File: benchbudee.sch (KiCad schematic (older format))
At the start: 0 parts

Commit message: Module 2 Unit 14
Defining Your Inputs and Outputs
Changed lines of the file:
@@
 LIBS:contrib
 LIBS:valves
-LIBS:benchbudee-block-cache
+LIBS:benchbudee-cache
 EELAYER 27 0
 EELAYER END
@@
 Sheet 1 8
 Title ""
-Date "1 feb 2014"
+Date "2 feb 2014"
 Rev ""
 Comp ""
@@
 $EndDescr
 $Sheet
-S 700  5100 3300 2250
+S 750  3950 3300 3000
 U 52ED26CD
 F0 "arduino" 50
 F1 "arduino.sch" 50
+F2 "Relay+" O R 4050 6700 60
+F3 "Relay-" I R 4050 6500 60
+F4 "MOSI" O R 4050 5500 60
+F5 "MISO" I R 4050 5700 60
+F6 "SCLK" O R 4050 5900 60
+F7 "CS_N" O R 4050 6100 60
+F8 "LED_EN" O R 4050 4900 60
+F9 "LED_FREQ" O R 4050 5100 60
+F10 "FAN_EN" O R 4050 4300 60
+F11 "TACH_MEAS" I R 4050 4500 60
 $EndSheet
 $Sheet
@@
 F2 "tc in +" I R 8250 4200 60
 F3 "tc in -" I R 8250 4400 60
+F4 "MOSI" I L 5550 4200 60
+F5 "MISO" O L 5550 4400 60
+F6 "SCLK" I L 5550 4600 60
+F7 "CS_N" I L 5550 4800 60
 $EndSheet
 $Sheet
@@
 F0 "relay" 50
 F1 "relay.sch" 50
+F2 "DIN+" I L 5550 5900 60
+F3 "DIN-" O L 5550 6100 60
+F4 "Relay+" I R 8250 5900 60
+F5 "Relay-" O R 8250 6100 60
 $EndSheet
 $Sheet
@@
 F0 "led driver" 50
 F1 "led driver.sch" 50
+F2 "EN" I L 5550 2600 60
+F3 "FREQ" I L 5550 2800 60
+F4 "String+" O R 8250 2600 60
+F5 "String-" I R 8250 2800 60
 $EndSheet
 $Sheet
@@
 F0 "fan controller" 50
 F1 "fan controller.sch" 50
+F2 "Power+" O R 8250 900 60
+F3 "Power-" I R 8250 1100 60
+F4 "Tach_out" O L 5550 1100 60
+F5 "Tach" I R 8250 1300 60
+F6 "Fan_in" I L 5550 900 60
 $EndSheet
 $Sheet

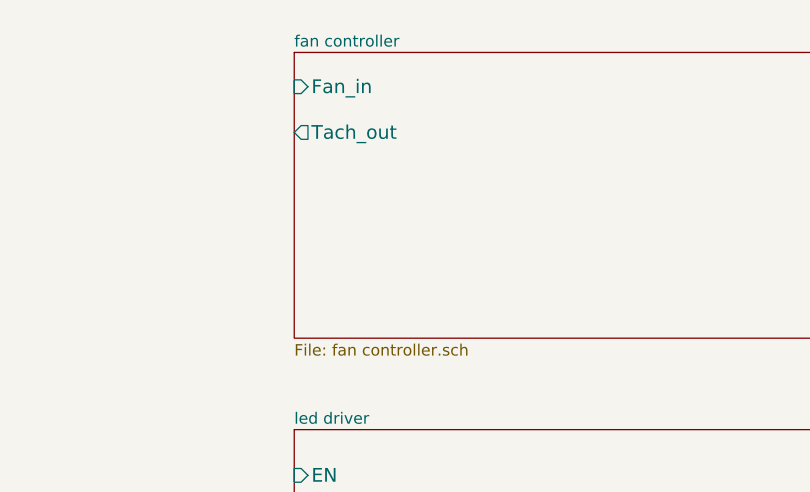
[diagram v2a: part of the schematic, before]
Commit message: Module 3 unit 4
Understanding The Current/Fan Driver Module
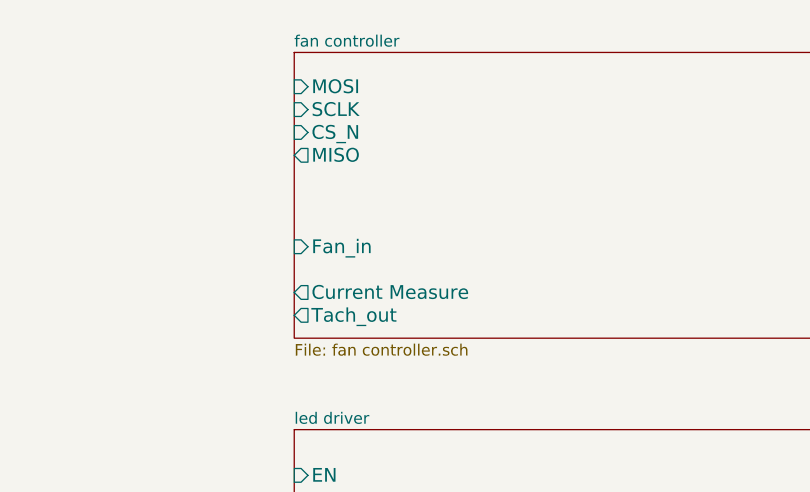
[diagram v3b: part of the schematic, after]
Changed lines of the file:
@@
 Sheet 1 8
 Title ""
-Date "8 feb 2014"
+Date "10 feb 2014"
 Rev ""
 Comp ""
@@
 F2 "Power+" O R 8250 900 60
 F3 "Power-" I R 8250 1100 60
-F4 "Tach_out" O L 5550 1100 60
+F4 "Tach_out" O L 5550 1900 60
 F5 "Tach" I R 8250 1300 60
-F6 "Fan_in" I L 5550 900 60
+F6 "Fan_in" I L 5550 1600 60
+F7 "Current Measure" O L 5550 1800 60
+F8 "MOSI" I L 5550 900 60
+F9 "MISO" O L 5550 1200 60
+F10 "CS_N" I L 5550 1100 60
+F11 "SCLK" I L 5550 1000 60
 $EndSheet
 $Sheet

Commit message: Module 3 Unit 5
Understanding The Relay Module
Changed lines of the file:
@@
 LIBS:contrib
 LIBS:valves
+LIBS:benchbudee
 LIBS:benchbudee-cache
 EELAYER 27 0
@@
 F2 "DIN+" I L 5550 5900 60
 F3 "DIN-" O L 5550 6100 60
-F4 "Relay+" I R 8250 5900 60
-F5 "Relay-" O R 8250 6100 60
+F4 "NC" B R 8250 6300 60
+F5 "NO" B R 8250 6500 60
+F6 "COM" B R 8250 6700 60
 $EndSheet
 $Sheet

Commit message: Module 3 Unit 6
Understanding The Power Protection And Filtering Module
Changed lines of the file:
@@
 $Descr A4 11693 8268
 encoding utf-8
-Sheet 1 8
+Sheet 1 9
 Title ""
 Date "10 feb 2014"
@@
 $EndSheet
 $Sheet
-S 5550 4050 2700 1250
+S 6600 4100 2700 1250
 U 52ED2725
 F0 "thermocouple" 50
 F1 "thermocouple.sch" 50
-F2 "tc in +" I R 8250 4200 60
-F3 "tc in -" I R 8250 4400 60
-F4 "MOSI" I L 5550 4200 60
-F5 "MISO" O L 5550 4400 60
-F6 "SCLK" I L 5550 4600 60
-F7 "CS_N" I L 5550 4800 60
+F2 "tc in +" I R 9300 4250 60
+F3 "tc in -" I R 9300 4450 60
+F4 "MOSI" I L 6600 4250 60
+F5 "MISO" O L 6600 4450 60
+F6 "SCLK" I L 6600 4650 60
+F7 "CS_N" I L 6600 4850 60
 $EndSheet
 $Sheet
-S 5550 5700 2700 1250
+S 6600 5750 2700 1250
 U 52ED273F
 F0 "relay" 50
 F1 "relay.sch" 50
-F2 "DIN+" I L 5550 5900 60
-F3 "DIN-" O L 5550 6100 60
-F4 "NC" B R 8250 6300 60
-F5 "NO" B R 8250 6500 60
-F6 "COM" B R 8250 6700 60
+F2 "DIN+" I L 6600 5950 60
+F3 "DIN-" O L 6600 6150 60
+F4 "NC" B R 9300 6350 60
+F5 "NO" B R 9300 6550 60
+F6 "COM" B R 9300 6750 60
 $EndSheet
 $Sheet
-S 700  700  3400 1900
+S 700  700  3350 1900
 U 52ED276F
 F0 "power" 50
@@
 $EndSheet
 $Sheet
-S 5550 2400 2700 1250
+S 6600 2450 2700 1250
 U 52ED27AA
 F0 "led driver" 50
 F1 "led driver.sch" 50
-F2 "EN" I L 5550 2600 60
-F3 "FREQ" I L 5550 2800 60
-F4 "String+" O R 8250 2600 60
-F5 "String-" I R 8250 2800 60
+F2 "EN" I L 6600 2650 60
+F3 "FREQ" I L 6600 2850 60
+F4 "String+" O R 9300 2650 60
+F5 "String-" I R 9300 2850 60
 $EndSheet
 $Sheet
-S 5550 750  2700 1250
+S 6600 800  2700 1250
 U 52ED27C5
 F0 "fan controller" 50
 F1 "fan controller.sch" 50
-F2 "Power+" O R 8250 900 60
-F3 "Power-" I R 8250 1100 60
-F4 "Tach_out" O L 5550 1900 60
-F5 "Tach" I R 8250 1300 60
-F6 "Fan_in" I L 5550 1600 60
-F7 "Current Measure" O L 5550 1800 60
-F8 "MOSI" I L 5550 900 60
-F9 "MISO" O L 5550 1200 60
-F10 "CS_N" I L 5550 1100 60
-F11 "SCLK" I L 5550 1000 60
+F2 "Power+" O R 9300 950 60
+F3 "Power-" I R 9300 1150 60
+F4 "Tach_out" O L 6600 1950 60
+F5 "Tach" I R 9300 1350 60
+F6 "Fan_in" I L 6600 1650 60
+F7 "Current Measure" O L 6600 1850 60
+F8 "MOSI" I L 6600 950 60
+F9 "MISO" O L 6600 1250 60
+F10 "CS_N" I L 6600 1150 60
+F11 "SCLK" I L 6600 1050 60
 $EndSheet
 $Sheet
-S 9500 750  1000 6200
+S 9900 800  1000 6200
 U 52ED27F4
 F0 "terminal block" 50
 F1 "terminal block.sch" 50
 $EndSheet
+$Sheet
+S 4300 700  2100 1900
+U 52F95312
+F0 "power adjustment monitor" 50
+F1 "power adjustment monitor.sch" 50
+$EndSheet
 $EndSCHEMATC

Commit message: Module 3 Unit 7
Understanding The Power Control, Conditioning And Monitoring Module
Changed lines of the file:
@@
 Sheet 1 9
 Title ""
-Date "10 feb 2014"
+Date "15 feb 2014"
 Rev ""
 Comp ""
@@
 $EndSheet
 $Sheet
-S 6600 4100 2700 1250
+S 6600 4450 2650 900
 U 52ED2725
 F0 "thermocouple" 50
 F1 "thermocouple.sch" 50
-F2 "tc in +" I R 9300 4250 60
-F3 "tc in -" I R 9300 4450 60
-F4 "MOSI" I L 6600 4250 60
-F5 "MISO" O L 6600 4450 60
-F6 "SCLK" I L 6600 4650 60
-F7 "CS_N" I L 6600 4850 60
+F2 "tc in +" I R 9250 4600 60
+F3 "tc in -" I R 9250 4800 60
+F4 "MOSI" I L 6600 4600 60
+F5 "MISO" O L 6600 4800 60
+F6 "SCLK" I L 6600 5000 60
+F7 "CS_N" I L 6600 5200 60
 $EndSheet
 $Sheet
-S 6600 5750 2700 1250
+S 6600 6050 2700 750
 U 52ED273F
 F0 "relay" 50
 F1 "relay.sch" 50
-F2 "DIN+" I L 6600 5950 60
-F3 "DIN-" O L 6600 6150 60
-F4 "NC" B R 9300 6350 60
-F5 "NO" B R 9300 6550 60
-F6 "COM" B R 9300 6750 60
+F2 "DIN+" I L 6600 6250 60
+F3 "DIN-" O L 6600 6450 60
+F4 "NC" B R 9300 6200 60
+F5 "NO" B R 9300 6400 60
+F6 "COM" B R 9300 6600 60
 $EndSheet
 $Sheet
@@
 $EndSheet
 $Sheet
-S 6600 2450 2700 1250
+S 6600 3050 2700 650
 U 52ED27AA
 F0 "led driver" 50
 F1 "led driver.sch" 50
-F2 "EN" I L 6600 2650 60
-F3 "FREQ" I L 6600 2850 60
-F4 "String+" O R 9300 2650 60
-F5 "String-" I R 9300 2850 60
+F2 "EN" I L 6600 3250 60
+F3 "FREQ" I L 6600 3450 60
+F4 "String+" O R 9300 3250 60
+F5 "String-" I R 9300 3450 60
 $EndSheet
 $Sheet
@@
 $EndSheet
 $Sheet
-S 4300 700  2100 1900
+S 4300 700  1800 1300
 U 52F95312
 F0 "power adjustment monitor" 50
 F1 "power adjustment monitor.sch" 50
+F2 "3V3_MON" O L 4300 1300 60
+F3 "5V_MON" O L 4300 1400 60
+F4 "V+ADJ_MON" O L 4300 1600 60
+F5 "V-ADJ_MON" O L 4300 1700 60
+F6 "V+CURRENT_MON" O L 4300 1800 60
+F7 "V-CURRENT_MON" O L 4300 1900 60
+F8 "V+ADJ" O R 6100 1300 60
+F9 "V-ADJ" O R 6100 1500 60
 $EndSheet
 $EndSCHEMATC

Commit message: Module 3 Unit 8
Understanding The LED Driver Module
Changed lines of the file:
@@
 F0 "led driver" 50
 F1 "led driver.sch" 50
-F2 "EN" I L 6600 3250 60
-F3 "FREQ" I L 6600 3450 60
-F4 "String+" O R 9300 3250 60
-F5 "String-" I R 9300 3450 60
+F2 "String+" O R 9300 3250 60
+F3 "String-" I R 9300 3450 60
+F4 "LED_EN_PWM" I L 6600 3250 60
 $EndSheet
 $Sheet

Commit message: Module 3 Unit 9
Understanding The Arduino Module
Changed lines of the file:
@@
 Sheet 1 9
 Title ""
-Date "15 feb 2014"
+Date "16 feb 2014"
 Rev ""
 Comp ""
@@
 $EndDescr
 $Sheet
-S 750  3950 3300 3000
+S 700  3050 3300 3750
 U 52ED26CD
 F0 "arduino" 50
 F1 "arduino.sch" 50
-F2 "Relay+" O R 4050 6700 60
-F3 "Relay-" I R 4050 6500 60
-F4 "MOSI" O R 4050 5500 60
-F5 "MISO" I R 4050 5700 60
-F6 "SCLK" O R 4050 5900 60
-F7 "CS_N" O R 4050 6100 60
-F8 "LED_EN" O R 4050 4900 60
-F9 "LED_FREQ" O R 4050 5100 60
-F10 "FAN_EN" O R 4050 4300 60
-F11 "TACH_MEAS" I R 4050 4500 60
-$EndSheet
-$Sheet
-S 6600 4450 2650 900
-U 52ED2725
-F0 "thermocouple" 50
-F1 "thermocouple.sch" 50
-F2 "tc in +" I R 9250 4600 60
-F3 "tc in -" I R 9250 4800 60
-F4 "MOSI" I L 6600 4600 60
-F5 "MISO" O L 6600 4800 60
-F6 "SCLK" I L 6600 5000 60
-F7 "CS_N" I L 6600 5200 60
+F2 "MOSI" O R 4000 3700 60
+F3 "MISO" I R 4000 3800 60
+F4 "SCLK" O R 4000 3900 60
+F5 "TACH_MEAS" I R 4000 4300 60
+F6 "Relay+" O R 4000 6500 60
+F7 "Relay-" O R 4000 6700 60
+F8 "Fan_En_N" O R 4000 4200 60
+F9 "Current_Measure" I R 4000 4400 60
+F10 "V+ADJ_MON" I R 4000 3200 60
+F11 "V-ADJ_MON" I R 4000 3300 60
+F12 "LED_EN_PWM" O R 4000 5300 60
+F13 "DAC_CS_N" O R 4000 4100 60
+F14 "ADC_CS_N" O R 4000 4000 60
 $EndSheet
 $Sheet
@@
 F0 "relay" 50
 F1 "relay.sch" 50
-F2 "DIN+" I L 6600 6250 60
-F3 "DIN-" O L 6600 6450 60
-F4 "NC" B R 9300 6200 60
-F5 "NO" B R 9300 6400 60
-F6 "COM" B R 9300 6600 60
+F2 "RELAY_NC" B R 9300 6400 60
+F3 "RELAY_NO" B R 9300 6600 60
+F4 "RELAY_COM" B R 9300 6200 60
+F5 "Relay+" I L 6600 6500 60
+F6 "Relay-" O L 6600 6700 60
 $EndSheet
 $Sheet
@@
 $EndSheet
 $Sheet
-S 6600 3050 2700 650
+S 6600 5050 2700 650
 U 52ED27AA
 F0 "led driver" 50
 F1 "led driver.sch" 50
-F2 "String+" O R 9300 3250 60
-F3 "String-" I R 9300 3450 60
-F4 "LED_EN_PWM" I L 6600 3250 60
-$EndSheet
-$Sheet
-S 6600 800  2700 1250
+F2 "LED_EN_PWM" I L 6600 5300 60
+F3 "LED_String+" O R 9300 5300 60
+F4 "LED_String-" O R 9300 5500 60
+$EndSheet
+$Sheet
+S 6600 3050 2700 1550
 U 52ED27C5
 F0 "fan controller" 50
 F1 "fan controller.sch" 50
-F2 "Power+" O R 9300 950 60
-F3 "Power-" I R 9300 1150 60
-F4 "Tach_out" O L 6600 1950 60
-F5 "Tach" I R 9300 1350 60
-F6 "Fan_in" I L 6600 1650 60
-F7 "Current Measure" O L 6600 1850 60
-F8 "MOSI" I L 6600 950 60
-F9 "MISO" O L 6600 1250 60
-F10 "CS_N" I L 6600 1150 60
-F11 "SCLK" I L 6600 1050 60
-$EndSheet
-$Sheet
-S 9900 800  1000 6200
+F2 "MOSI" I L 6600 3200 60
+F3 "MISO" O L 6600 3300 60
+F4 "CS_N" I L 6600 3500 60
+F5 "SCLK" I L 6600 3400 60
+F6 "Fan_Out+" O R 9300 3200 60
+F7 "Tach_In" I R 9300 3600 60
+F8 "Tach_Meas" O L 6600 4300 60
+F9 "Fan_En_N" I L 6600 4200 60
+F10 "Current_Measure" O L 6600 4400 60
+F11 "Fan_Out-" O R 9300 3400 60
+$EndSheet
+$Sheet
+S 9900 800  1000 6000
 U 52ED27F4
 F0 "terminal block" 50
 F1 "terminal block.sch" 50
-$EndSheet
-$Sheet
-S 4300 700  1800 1300
+F2 "Tach_In" O L 9900 3600 60
+F3 "LED_String+" O L 9900 5300 60
+F4 "LED_String-" O L 9900 5500 60
+F5 "Fan_Out+" O L 9900 3200 60
+F6 "Fan_Out-" O L 9900 3400 60
+F7 "V+ADJ" I L 9900 1150 60
+F8 "V-ADJ" I L 9900 1350 60
+F9 "TC_IN+" I L 9900 2100 60
+F10 "TC_IN-" I L 9900 2300 60
+F11 "RELAY_COM" B L 9900 6200 60
+F12 "RELAY_NC" B L 9900 6400 60
+F13 "RELAY_NO" B L 9900 6600 60
+$EndSheet
+$Sheet
+S 6600 800  2700 900
 U 52F95312
 F0 "power adjustment monitor" 50
 F1 "power adjustment monitor.sch" 50
-F2 "3V3_MON" O L 4300 1300 60
-F3 "5V_MON" O L 4300 1400 60
-F4 "V+ADJ_MON" O L 4300 1600 60
-F5 "V-ADJ_MON" O L 4300 1700 60
-F6 "V+CURRENT_MON" O L 4300 1800 60
-F7 "V-CURRENT_MON" O L 4300 1900 60
-F8 "V+ADJ" O R 6100 1300 60
-F9 "V-ADJ" O R 6100 1500 60
-$EndSheet
+F2 "3V3_MON" O L 6600 900 60
+F3 "5V_MON" O L 6600 1000 60
+F4 "V+ADJ_MON" O L 6600 1200 60
+F5 "V-ADJ_MON" O L 6600 1300 60
+F6 "V+CURRENT_MON" O L 6600 1400 60
+F7 "V-CURRENT_MON" O L 6600 1500 60
+F8 "V+ADJ" O R 9300 1150 60
+F9 "V-ADJ" O R 9300 1350 60
+$EndSheet
+$Sheet
+S 6600 1950 2700 900
+U 52ED2725
+F0 "thermocouple" 50
+F1 "thermocouple.sch" 50
+F2 "MOSI" I L 6600 2100 60
+F3 "MISO" O L 6600 2200 60
+F4 "SCLK" I L 6600 2300 60
+F5 "CS_N" I L 6600 2400 60
+F6 "TC_IN+" I R 9300 2100 60
+F7 "TC_IN-" I R 9300 2300 60
+$EndSheet
+Wire Wire Line
+	9300 6200 9900 6200
+Wire Wire Line
+	9900 6400 9300 6400
+Wire Wire Line
+	9300 6600 9900 6600
+Wire Wire Line
+	9300 1150 9900 1150
+Wire Wire Line
+	9900 1350 9300 1350
+Wire Wire Line
+	9300 5300 9900 5300
+Wire Wire Line
+	9300 5500 9900 5500
+Wire Wire Line
+	4000 3200 4500 3200
+Wire Wire Line
+	4500 3200 4500 1200
+Wire Wire Line
+	4500 1200 6600 1200
+Wire Wire Line
+	6600 1300 4600 1300
+Wire Wire Line
+	4600 1300 4600 3300
+Wire Wire Line
+	4600 3300 4000 3300
+Wire Wire Line
+	9900 2100 9300 2100
+Wire Wire Line
+	9300 2300 9900 2300
+Wire Wire Line
+	9900 3200 9300 3200
+Wire Wire Line
+	9300 3400 9900 3400
+Wire Wire Line
+	9900 3600 9300 3600
+Wire Wire Line
+	4000 3700 4700 3700
+Wire Wire Line
+	4700 3700 4700 2100
+Wire Wire Line
+	4700 2100 6600 2100
+Wire Wire Line
+	6600 2200 4800 2200
+Wire Wire Line
+	4800 2200 4800 3800
+Wire Wire Line
+	4800 3800 4000 3800
+Wire Wire Line
+	4000 3900 4900 3900
+Wire Wire Line
+	4900 3900 4900 2300
+Wire Wire Line
+	4900 2300 6600 2300
+Wire Wire Line
+	4000 4200 6600 4200
+Wire Wire Line
+	4000 4300 6600 4300
+Wire Wire Line
+	4000 4400 6600 4400
+Wire Wire Line
+	6600 3200 4700 3200
+Connection ~ 4700 3200
+Wire Wire Line
+	6600 3300 4800 3300
+Connection ~ 4800 3300
+Wire Wire Line
+	6600 3400 4900 3400
+Connection ~ 4900 3400
+Wire Wire Line
+	4000 4000 5000 4000
+Wire Wire Line
+	5000 4000 5000 2400
+Wire Wire Line
+	5000 2400 6600 2400
+Wire Wire Line
+	4000 4100 5100 4100
+Wire Wire Line
+	5100 4100 5100 3500
+Wire Wire Line
+	5100 3500 6600 3500
+Wire Wire Line
+	6600 5300 4000 5300
+Wire Wire Line
+	4000 6500 6600 6500
+Wire Wire Line
+	6600 6700 4000 6700
 $EndSCHEMATC
